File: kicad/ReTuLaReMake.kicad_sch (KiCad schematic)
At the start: 23 parts, among them J1 40 Pin DIP Header, J2 Conn_02x05_Odd_Even, U1 ATF1508AS-10AU100

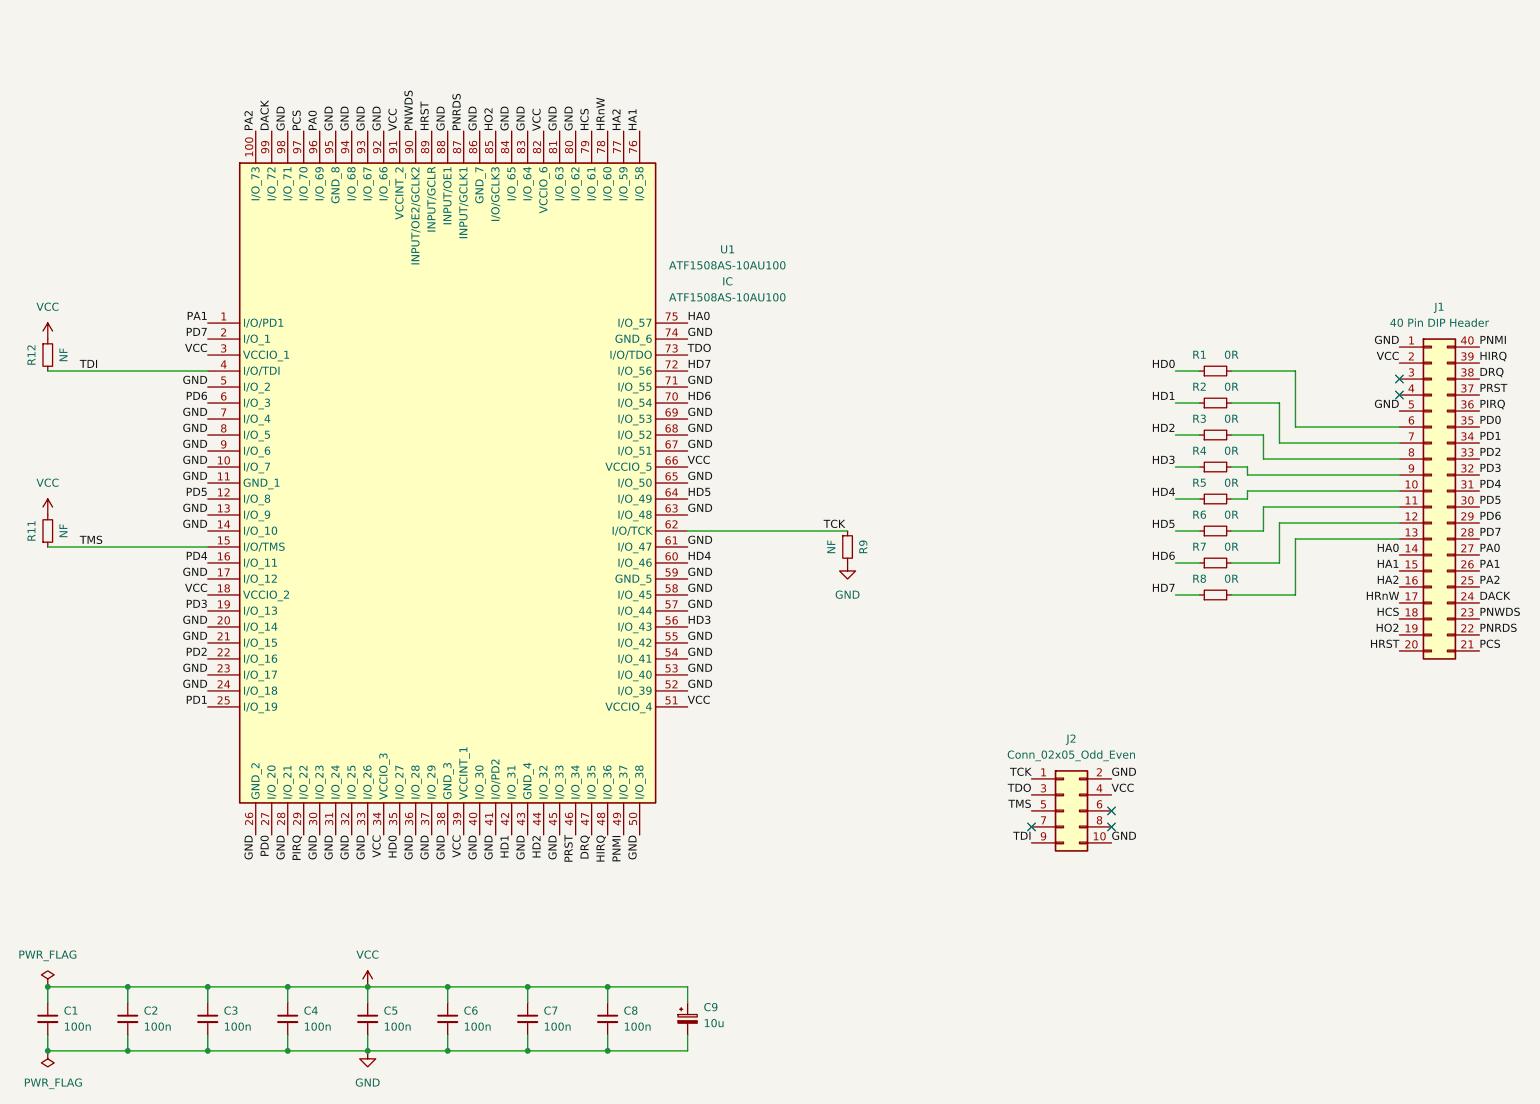
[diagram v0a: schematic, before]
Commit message: KiCAD: Add schottky diodes
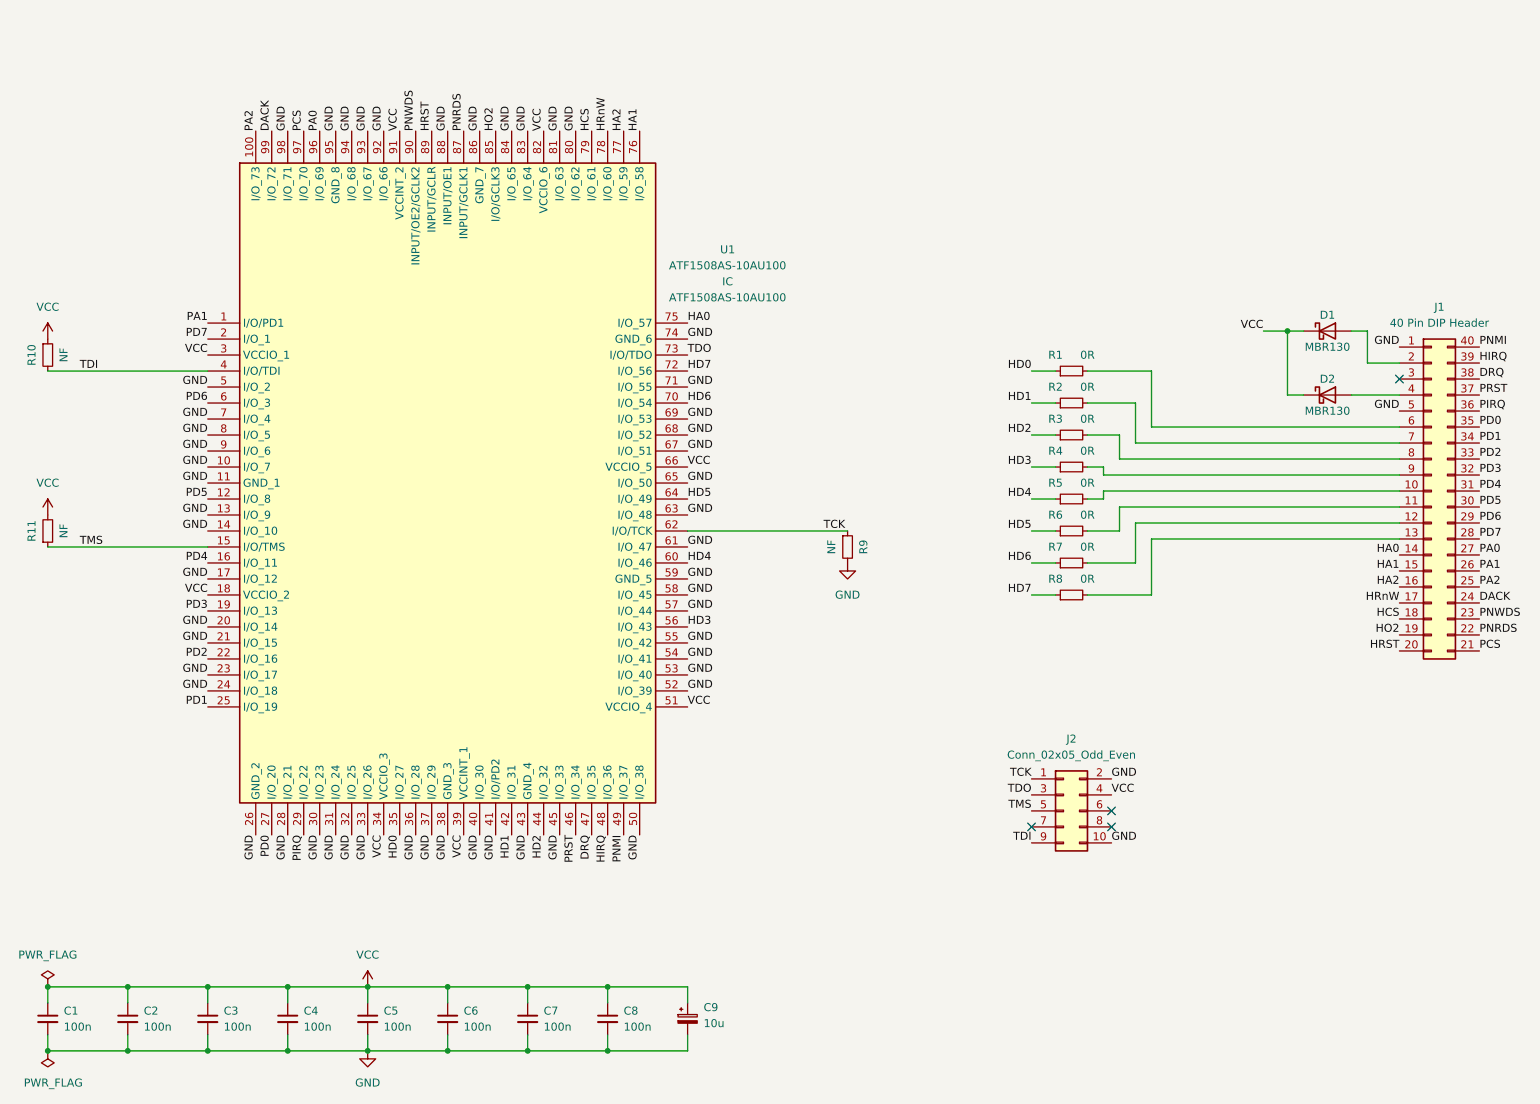
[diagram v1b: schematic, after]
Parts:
- added D1, D2: MBR130, Diode_SMD:D_SOD-123, symbol Device:D_Schottky
- renumbered R12 to R10
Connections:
- net VCC: now also D1.1 (K), D2.1 (K); no longer J1.2 (Pin_2)
- net at J1.4 (Pin_4): now also D2.2 (A)
- new net: D1.2 (A), J1.2 (Pin_2)
- no-connect marks 5 -> 4
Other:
- moved on the sheet: R1, R2, R3, R4, R5, R6, R7, R8

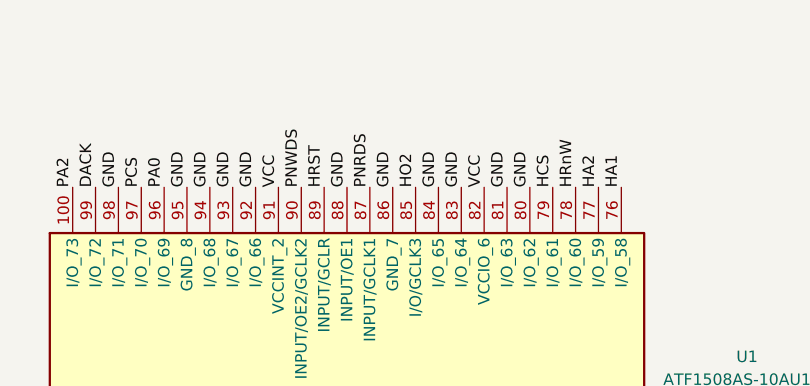
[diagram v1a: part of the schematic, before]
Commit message: KiCAD: Add 12V OE1 Test Point
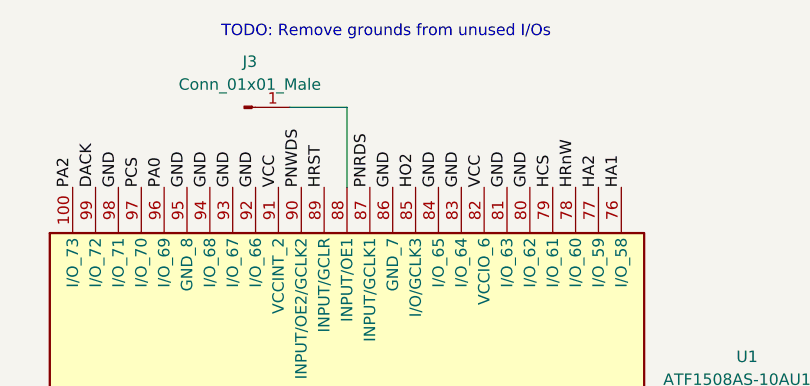
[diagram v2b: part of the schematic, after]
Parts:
- added J3: Conn_01x01_Male, Connector_PinHeader_2.54mm:PinHeader_1x01_P2.54mm_Vertical, symbol Connector:Conn_01x01_Male
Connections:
- net GND: no longer U1.88 (INPUT/OE1)
- new net: J3.1 (Pin_1), U1.88 (INPUT/OE1)
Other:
- note added: "TODO: Remove grounds from unused I/Os"
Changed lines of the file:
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@@
+    (stroke (width 0) (type default) (color 0 0 0 0))
+  )
+  (wire (pts (xy 104.14 29.21) (xy 104.14 38.1))
     (stroke (width 0) (type default) (color 0 0 0 0))
   )
@@
     (stroke (width 0) (type default) (color 0 0 0 0))
   )
+  (wire (pts (xy 97.79 29.21) (xy 104.14 29.21))
+    (stroke (width 0) (type default) (color 0 0 0 0))
+  )
   (wire (pts (xy 215.9 102.87) (xy 215.9 111.76))
     (stroke (width 0) (type default) (color 0 0 0 0))
@@
     (stroke (width 0) (type default) (color 0 0 0 0))
   )
+  (text "TODO: Remove grounds from unused I/Os" (at 90.17 21.59 0)
+    (effects (font (size 1.27 1.27)) (justify left bottom))
+  )
   (label "PD6" (at 267.97 100.33 0)
     (effects (font (size 1.27 1.27)) (justify left bottom))
@@
   (label "PD5" (at 66.04 96.52 180)
     (effects (font (size 1.27 1.27)) (justify right bottom))
-  )
-  (label "GND" (at 104.14 38.1 90)
-    (effects (font (size 1.27 1.27)) (justify left bottom))
   )
   (label "HD0" (at 96.52 149.86 270)
@@
     (pin "2")
   )
+  (symbol (lib_id "Connector:Conn_01x01_Male") (at 92.71 29.21 0) (unit 1)
+    (in_bom yes) (on_board yes) (fields_autoplaced)
+    (property "Reference" "J3" (id 0) (at 93.345 24.13 0))
+    (property "Value" "Conn_01x01_Male" (id 1) (at 93.345 26.67 0))
+    (property "Footprint" "Connector_PinHeader_2.54mm:PinHeader_1x01_P2.54mm_Vertical" (id 2) (at 92.71 29.21 0)
+      (effects (font (size 1.27 1.27)) hide)
+    )
+    (property "Datasheet" "~" (id 3) (at 92.71 29.21 0)
+      (effects (font (size 1.27 1.27)) hide)
+    )
+    (pin "1")
+  )
   (symbol (lib_id "Device:R_Small") (at 203.2 106.68 90) (unit 1)
     (in_bom yes) (on_board yes)
@@
       (reference "J2") (unit 1) (value "Conn_02x05_Odd_Even") (footprint "Connector_PinHeader_2.54mm:PinHeader_2x05_P2.54mm_Vertical")
     )
+    (path "/f6e4cde9-e72b-4bbf-bea7-fc857ecbbbf9"
+      (reference "J3") (unit 1) (value "Conn_01x01_Male") (footprint "Connector_PinHeader_2.54mm:PinHeader_1x01_P2.54mm_Vertical")
+    )
     (path "/964de713-4bf4-4d62-9515-7459808eb087"

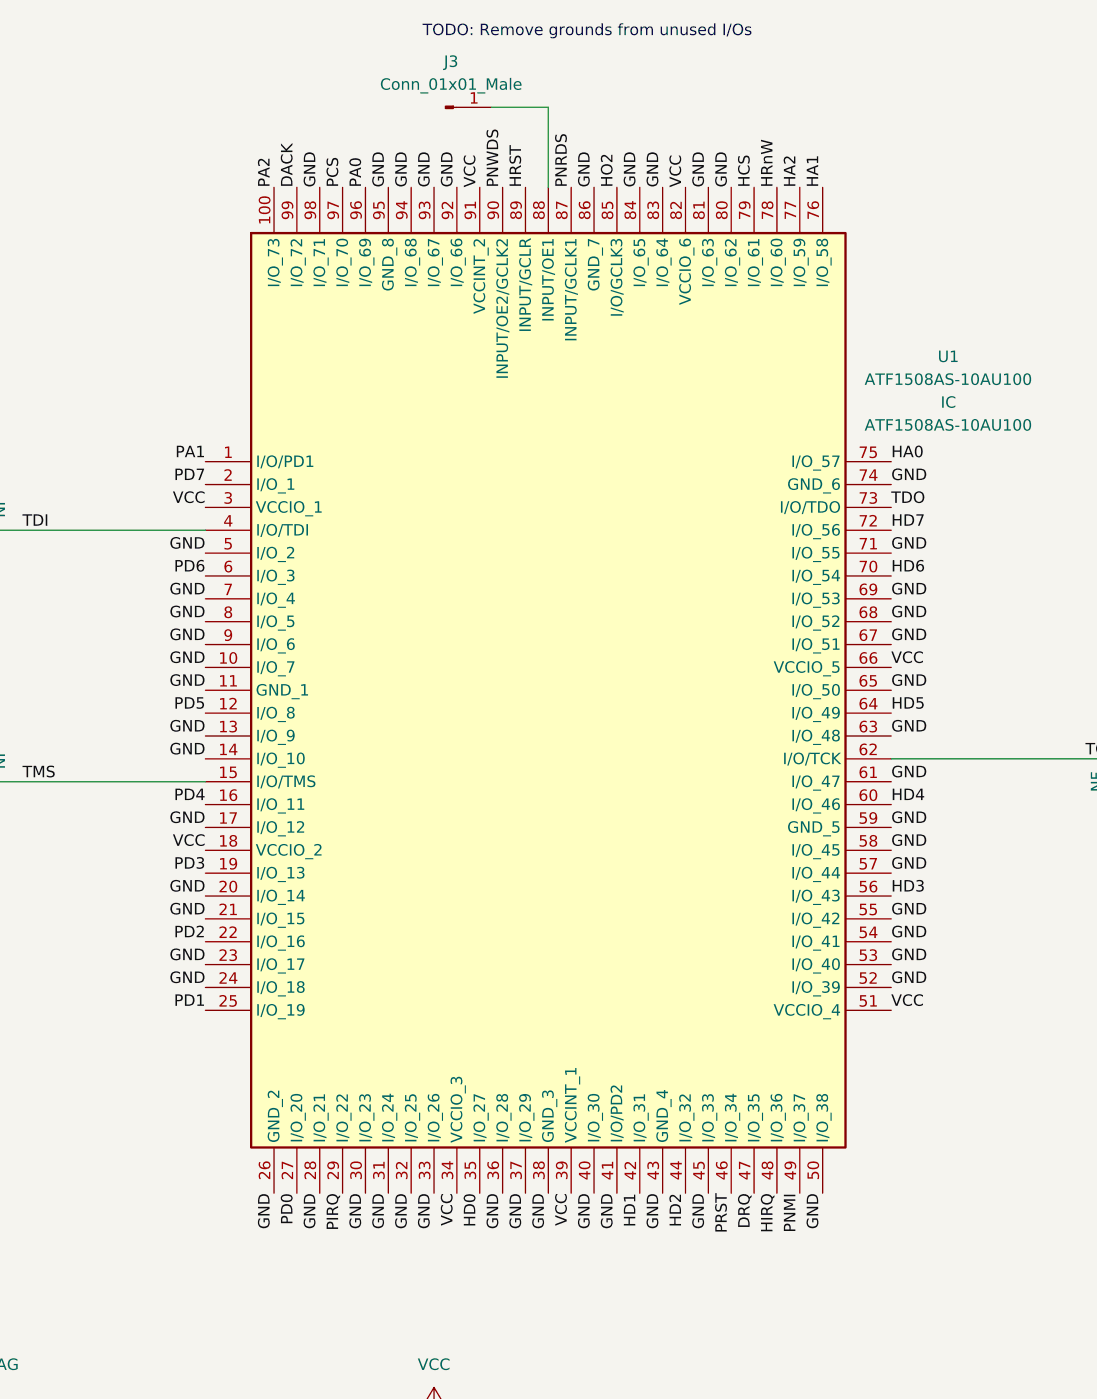
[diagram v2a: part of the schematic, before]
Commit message: KiCAD: Remove GNDs on unused I/Os
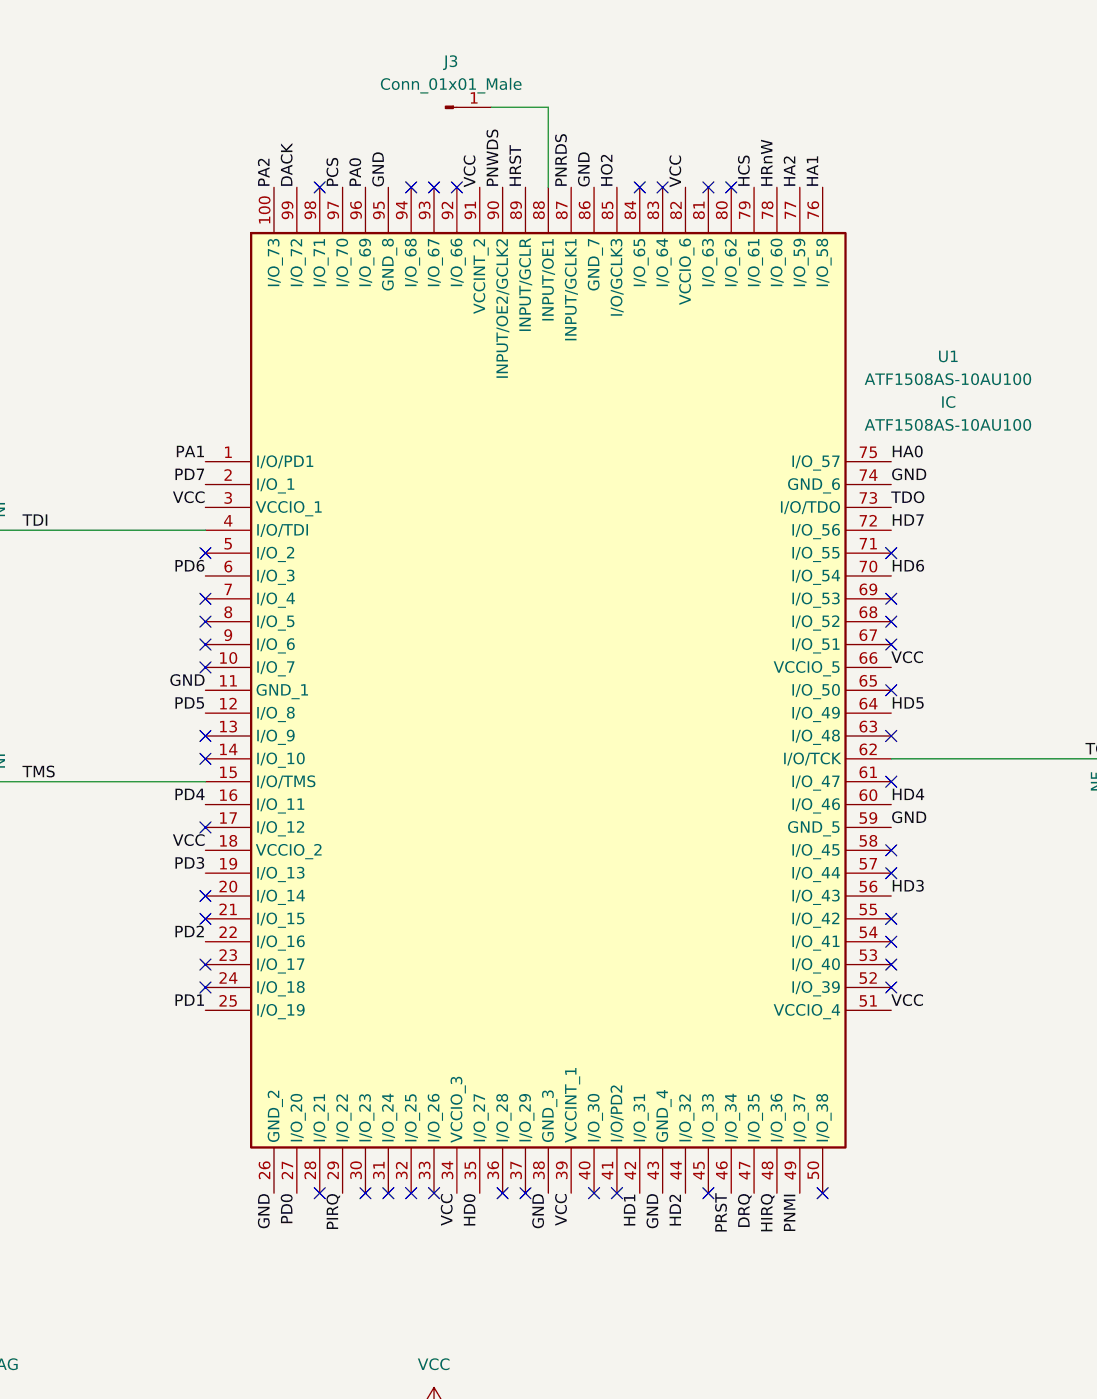
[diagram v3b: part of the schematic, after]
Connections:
- net GND: no longer U1.10 (I/O_7), U1.13 (I/O_9), U1.14 (I/O_10), U1.17 (I/O_12), U1.20 (I/O_14), U1.21 (I/O_15), U1.23 (I/O_17), U1.24 (I/O_18), U1.28 (I/O_21), U1.30 (I/O_23), U1.31 (I/O_24), U1.32 (I/O_25), U1.33 (I/O_26), U1.36 (I/O_28), U1.37 (I/O_29), U1.40 (I/O_30), U1.41 (I/O/PD2), U1.45 (I/O_33), U1.5 (I/O_2), U1.50 (I/O_38), U1.52 (I/O_39), U1.53 (I/O_40), U1.54 (I/O_41), U1.55 (I/O_42), U1.57 (I/O_44), U1.58 (I/O_45), U1.61 (I/O_47), U1.63 (I/O_48), U1.65 (I/O_50), U1.67 (I/O_51), U1.68 (I/O_52), U1.69 (I/O_53), U1.7 (I/O_4), U1.71 (I/O_55), U1.8 (I/O_5), U1.80 (I/O_62), U1.81 (I/O_63), U1.83 (I/O_64), U1.84 (I/O_65), U1.9 (I/O_6), U1.92 (I/O_66), U1.93 (I/O_67), U1.94 (I/O_68), U1.98 (I/O_71)
- no-connect marks 4 -> 48
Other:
- note removed: "TODO: Remove grounds from unused I/Os"
